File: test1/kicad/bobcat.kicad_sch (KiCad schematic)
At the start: 0 parts

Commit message: test1: fill in Power, Bias, Bobcat, Connectors, FMC sheets
Completes the test1 Bobcat carrier hierarchical schematic. All 7 sheets
(root + 6 children) parse cleanly with kicad-cli and render to SVG/PDF.

Contents per child:
  - power.kicad_sch       — TPS7A8401A LDO (3P3V → 0.8V via ANY-OUT
                            strap, OUT side fans to +VDDD/+VDDA1/+VDDA2
                            via 1×2 jumpers) + TPS22916 load switch
                            (VADJ → +VDDIO) with EN pulldowns + decoupling.
  - bobcat.kicad_sch      — Bobcat 40-QFN DUT with VDDD/VDDIO decoupling,
                            VDDA1/VDDA2 series 0Ω + decoupling, hier-label
                            exits on all four edges for SAMPLE_OUT*,
                            SPI, GPIO, CLK_OUT*, BIAS0/1, etc.
  - eeprom.kicad_sch      — 24AA08 I²C EEPROM (address 000, WP→GND,
                            0.1 µF decoupling, 2.2 kΩ I²C pull-ups).
  - bias.kicad_sch        — MCP4728 quad DAC + OPA2388 dual op-amp
                            (units 1 & 2) + PMZ1200UPEYL high-side PMOS
                            × 2 channels + 5.11 kΩ 0.1% sense resistors +
                            DNP 2N7002 isolation NMOS placeholders.
  - connectors.kicad_sch  — 4× SMA for CLK_OUT0–3, 3× SMA for
                            OSC_EN/WEIGHT_EN/SAMPLE_TRIG, 1×4 GPIO
                            header, 3× Keystone-5011 GND test clips.
  - fmc.kicad_sch         — VITA 57.1 LPC connector (4 units × 40 pins),
                            wired for 3P3V/VADJ/SCL/SDA/PRSNT/GA0/GA1/
                            PG_C2M/LDO_EN/LSW_EN; LA-bank pins NC'd for
                            later pinning; all other C/D/G/H pins to GND.

Generator improvements driven by this round:
  - Multi-unit symbol support (parse_pins now returns the per-pin unit
    number; place() takes a unit= parameter and emits matching (unit N)
    in the instance + path).
  - Escape backslash/quote in property values so refs/values with
    embedded " (e.g. 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
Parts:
- added C1, C3, C4, C5: 0.1uF, Capacitor_SMD:C_0402_1005Metric, symbol Device:C
- added C2, C6: 1uF, Capacitor_SMD:C_0402_1005Metric, symbol Device:C
- added R5, R6: 0, Resistor_SMD:R_0402_1005Metric, symbol Device:R
- added U1: Bobcat, Bobcat:QFN-40_5x5mm_P0.4mm_EP3.5mm, symbol Lib:Bobcat
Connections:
- new net: C4.1, R6.1, U1.26 (VDDA2), U1.27 (VDDA2)
- new net: C3.1, R5.2, U1.1 (VDDA1)
- new net +VDDA1: R5.1
- new net +VDDA2: R6.2
- new net +VDDD: C1.1, C2.1, U1.12 (VDDD), U1.20 (VDDD)
- new net +VDDIO: C5.1, C6.1, U1.13 (VDDIO), U1.22 (VDDIO), U1.33 (VDDIO), U1.34 (VDDIO), U1.7 (VDDIO)
- new net BIAS0: U1.28 (BIAS0)
- new net BIAS1: U1.29 (BIAS1)
- new net CLK_OUT0: U1.36 (CLK_OUT0)
- new net CLK_OUT1: U1.35 (CLK_OUT1)
- new net CLK_OUT2: U1.32 (CLK_OUT2)
- new net CLK_OUT3: U1.31 (CLK_OUT3)
- new net CS_L: U1.17 (CS_L)
- new net GND: C1.2, C2.2, C3.2, C4.2, C5.2, C6.2, U1.41 (GND)
- new net GPIO0: U1.40 (GPIO0)
- new net GPIO1: U1.39 (GPIO1)
- new net GPIO2: U1.38 (GPIO2)
- new net GPIO3: U1.37 (GPIO3)
- new net MISO: U1.15 (MISO)
- new net MOSI: U1.14 (MOSI)
- new net OSC_EN: U1.23 (OSC_EN)
- new net RESET_N: U1.19 (RESET_N)
- new net SAMPLE_OUT0: U1.3 (SAMPLE_OUT0)
- new net SAMPLE_OUT1: U1.4 (SAMPLE_OUT1)
- new net SAMPLE_OUT2: U1.5 (SAMPLE_OUT2)
- new net SAMPLE_OUT3: U1.6 (SAMPLE_OUT3)
- new net SAMPLE_OUT4: U1.8 (SAMPLE_OUT4)
- new net SAMPLE_OUT5: U1.9 (SAMPLE_OUT5)
- new net SAMPLE_OUT6: U1.10 (SAMPLE_OUT6)
- new net SAMPLE_OUT7: U1.11 (SAMPLE_OUT7)
- new net SAMPLE_OUTV: U1.2 (SAMPLE_OUTV)
- new net SAMPLE_TRIG: U1.25 (SAMPLE_TRIG)
- new net SCLK: U1.16 (SCLK)
- new net SPI_DMODE: U1.18 (SPI_DMODE)
- new net WEIGHT_EN: U1.24 (WEIGHT_EN)
- no-connect marks 0 -> 2

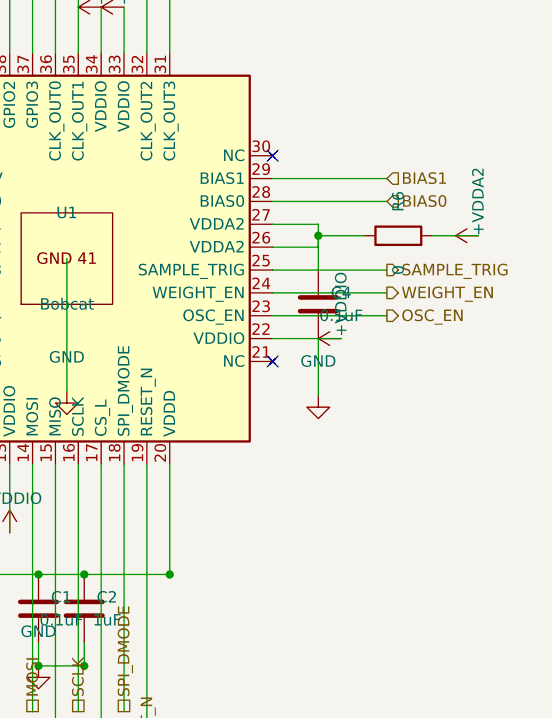
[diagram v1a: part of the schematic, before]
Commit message: Apply layout best-practices from reference schematic
Skill updates (from the LTC3114 reference sample):
  - New rule 5: no net passes through a component body (visual ambiguity).
  - New rule 6: every placed component is in-path or removed — DNP parts
    stay wired in series and just carry (dnp yes) + "DNP" value tag; never
    leave a part with no_connect on all its pins as a "for later"
    placeholder.
  - New rule 7: GND symbols cluster — one (power:GND) per local pin group,
    not one per pin. Connector banks bus their GNDs onto a single rail
    with one terminating triangle.
  - New rule 8: canonical decoupling-cap cluster (bulk+HF share one rail
    above and one GND below; stay off the path of unrelated nets).

test1 design fixes (each addresses a specific point raised on review):

  1. Bias: Q3, Q4 (2N7002 NMOS isolators) now wired in series between
     each PMOS drain and the BIASx output — gates exit as BIAS_ISO0 /
     BIAS_ISO1 hier labels for MCU control. Marked DNP via "2N7002 DNP"
     value. No more orphaned no_connects.

  2. Bobcat: VDDA2 decoupling cap C4 moved onto its own branch BELOW the
     R6 series-0Ω lane, off the pin-26/27 tie wire path.

  3. FMC: ~150 individual per-pin GND symbols collapsed into one
     consolidated GND rail per unit (J1/J2/J3/J4), each terminating in a
     single GND triangle at the rail's bottom.

  4. Power: TPS22916 (U2) decoupling caps C6 and C7 moved ALONGSIDE the
     chip body (left and right) at the same y as VIN/VOUT — wires no
     longer pass under the chip footprint. Cap pin 1 (top) → chip pin
     via horizontal stub; cap pin 2 (bot) → GND rail below.

Co-Authored-By: Claude Opus 4.7 (1M context) <noreply@anthropic.com>
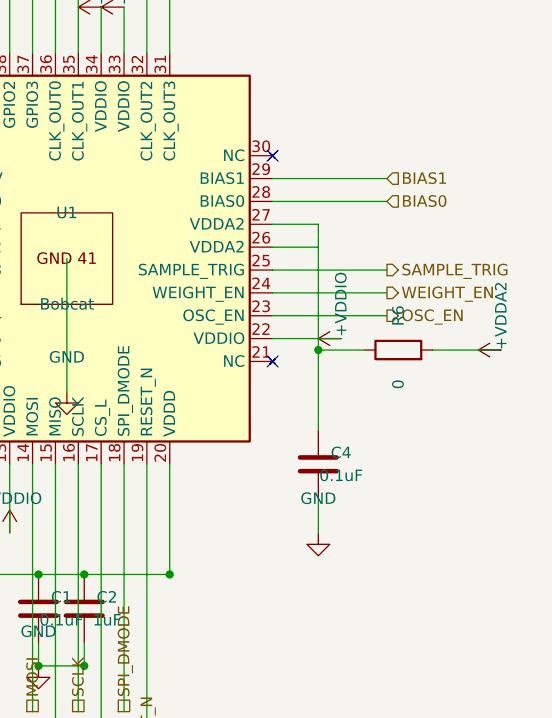
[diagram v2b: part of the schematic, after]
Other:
- moved on the sheet: C4, R6
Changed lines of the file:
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@@
   (wire (pts (xy 222.86 126.19) (xy 227.94000000000003 126.19)) (stroke (width 0) (type default)))
   (wire (pts (xy 227.94000000000003 128.73) (xy 227.94000000000003 126.19)) (stroke (width 0) (type default)))
+  (wire (pts (xy 227.94000000000003 128.73) (xy 227.94000000000003 140.16)) (stroke (width 0) (type default)))
   (symbol
     (lib_id "Device:R")
-    (at 236.83 127.46 90)
+    (at 236.83 140.16 90)
     (unit 1) (in_bom yes) (on_board yes) (dnp no)
-    (property "Reference" "R6" (at 236.83 123.64999999999999 0) (effects (font (size 1.27 1.27))))
-    (property "Value" "0" (at 236.83 131.26999999999998 0) (effects (font (size 1.27 1.27))))
+    (property "Reference" "R6" (at 236.83 136.35 0) (effects (font (size 1.27 1.27))))
+    (property "Value" "0" (at 236.83 143.97 0) (effects (font (size 1.27 1.27))))
     (property "Footprint" "Resistor_SMD:R_0402_1005Metric" (at 0 0 0) (effects (font (size 1.27 1.27)) (hide yes)))
     (property "Datasheet" "" (at 0 0 0) (effects (font (size 1.27 1.27)) (hide yes)))
@@
       (project "test1"
         (path "/4ed7a046-ef33-57d9-8730-321c05965af3/e6b90fa2-2dfc-5319-a99a-2ebf8a1933a0" (reference "R6") (unit 1)))))
-  (wire (pts (xy 227.94000000000003 127.46) (xy 233.02 127.46)) (stroke (width 0) (type default)))
-  (wire (pts (xy 240.64000000000001 127.46) (xy 245.72000000000003 127.46)) (stroke (width 0) (type default)))
+  (wire (pts (xy 227.94000000000003 140.16) (xy 233.02 140.16)) (stroke (width 0) (type default)))
+  (wire (pts (xy 240.64000000000001 140.16) (xy 248.26000000000002 140.16)) (stroke (width 0) (type default)))
   (symbol
     (lib_id "power:+VDDA2")
-    (at 245.72000000000003 127.46 90)
+    (at 248.26000000000002 140.16 90)
     (unit 1) (in_bom yes) (on_board yes) (dnp no)
-    (property "Reference" "#PWRc1e63a9b" (at 245.72000000000003 121.11 0) (effects (font (size 1.27 1.27)) (hide yes)))
-    (property "Value" "+VDDA2" (at 245.72000000000003 123.64999999999999 0) (effects (font (size 1.27 1.27))))
+    (property "Reference" "#PWRf1cae80c" (at 248.26000000000002 133.81 0) (effects (font (size 1.27 1.27)) (hide yes)))
+    (property "Value" "+VDDA2" (at 248.26000000000002 136.35 0) (effects (font (size 1.27 1.27))))
     (property "Footprint" "" (at 0 0 0) (effects (font (size 1.27 1.27)) (hide yes)))
     (property "Datasheet" "" (at 0 0 0) (effects (font (size 1.27 1.27)) (hide yes)))
@@
     (instances
       (project "test1"
-        (path "/4ed7a046-ef33-57d9-8730-321c05965af3/e6b90fa2-2dfc-5319-a99a-2ebf8a1933a0" (reference "#PWRc1e63a9b") (unit 1)))))
+        (path "/4ed7a046-ef33-57d9-8730-321c05965af3/e6b90fa2-2dfc-5319-a99a-2ebf8a1933a0" (reference "#PWRf1cae80c") (unit 1)))))
   (symbol
     (lib_id "Device:C")
-    (at 227.94000000000003 135.07999999999998 0)
+    (at 227.94000000000003 152.85999999999999 0)
     (unit 1) (in_bom yes) (on_board yes) (dnp no)
-    (property "Reference" "C4" (at 230.48000000000002 133.80999999999997 0) (effects (font (size 1.27 1.27))))
-    (property "Value" "0.1uF" (at 230.48000000000002 136.35 0) (effects (font (size 1.27 1.27))))
+    (property "Reference" "C4" (at 230.48000000000002 151.58999999999997 0) (effects (font (size 1.27 1.27))))
+    (property "Value" "0.1uF" (at 230.48000000000002 154.13 0) (effects (font (size 1.27 1.27))))
     (property "Footprint" "Capacitor_SMD:C_0402_1005Metric" (at 0 0 0) (effects (font (size 1.27 1.27)) (hide yes)))
     (property "Datasheet" "" (at 0 0 0) (effects (font (size 1.27 1.27)) (hide yes)))
@@
       (project "test1"
         (path "/4ed7a046-ef33-57d9-8730-321c05965af3/e6b90fa2-2dfc-5319-a99a-2ebf8a1933a0" (reference "C4") (unit 1)))))
-  (wire (pts (xy 227.94000000000003 131.26999999999998) (xy 227.94000000000003 127.46)) (stroke (width 0) (type default)))
-  (junction (at 227.94000000000003 127.46) (diameter 0) (color 0 0 0 0))
-  (wire (pts (xy 227.94000000000003 138.89) (xy 227.94000000000003 145.24)) (stroke (width 0) (type default)))
+  (junction (at 227.94000000000003 140.16) (diameter 0) (color 0 0 0 0))
+  (wire (pts (xy 227.94000000000003 140.16) (xy 227.94000000000003 149.04999999999998)) (stroke (width 0) (type default)))
+  (wire (pts (xy 227.94000000000003 156.67) (xy 227.94000000000003 160.48)) (stroke (width 0) (type default)))
   (symbol
     (lib_id "power:GND")
-    (at 227.94000000000003 145.24 0)
+    (at 227.94000000000003 160.48 0)
     (unit 1) (in_bom yes) (on_board yes) (dnp no)
-    (property "Reference" "#PWRcd432e56" (at 227.94000000000003 138.89000000000001 0) (effects (font (size 1.27 1.27)) (hide yes)))
-    (property "Value" "GND" (at 227.94000000000003 141.43 0) (effects (font (size 1.27 1.27))))
+    (property "Reference" "#PWRb5cd5e9b" (at 227.94000000000003 154.13 0) (effects (font (size 1.27 1.27)) (hide yes)))
+    (property "Value" "GND" (at 227.94000000000003 156.67 0) (effects (font (size 1.27 1.27))))
     (property "Footprint" "" (at 0 0 0) (effects (font (size 1.27 1.27)) (hide yes)))
     (property "Datasheet" "" (at 0 0 0) (effects (font (size 1.27 1.27)) (hide yes)))
@@
     (instances
       (project "test1"
-        (path "/4ed7a046-ef33-57d9-8730-321c05965af3/e6b90fa2-2dfc-5319-a99a-2ebf8a1933a0" (reference "#PWRcd432e56") (unit 1)))))
+        (path "/4ed7a046-ef33-57d9-8730-321c05965af3/e6b90fa2-2dfc-5319-a99a-2ebf8a1933a0" (reference "#PWRb5cd5e9b") (unit 1)))))
   (wire (pts (xy 177.14 133.81) (xy 169.51999999999998 133.81)) (stroke (width 0) (type default)))
   (symbol
